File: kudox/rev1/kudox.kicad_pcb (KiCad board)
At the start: 2 copper layers, 143.6 x 129.5 mm, 81 parts, among them K0 KEYSW, K1 KEYSW, K10 KEYSW, K11 KEYSW, K12 KEYSW, K13 KEYSW, K14 KEYSW, K15 KEYSW, K16 KEYSW, K2 KEYSW, K20 KEYSW, K21 KEYSW, K22 KEYSW, K23 KEYSW, K24 KEYSW, K25 KEYSW, K3 KEYSW, K30 KEYSW, K31 KEYSW, K32 KEYSW, K33 KEYSW, K34 KEYSW, K35 KEYSW, K4 KEYSW, K40 KEYSW, K41 KEYSW, K42 KEYSW, K43 KEYSW, K44 KEYSW, K45 KEYSW, K46 KEYSW, K5 KEYSW, U1 ProMicro

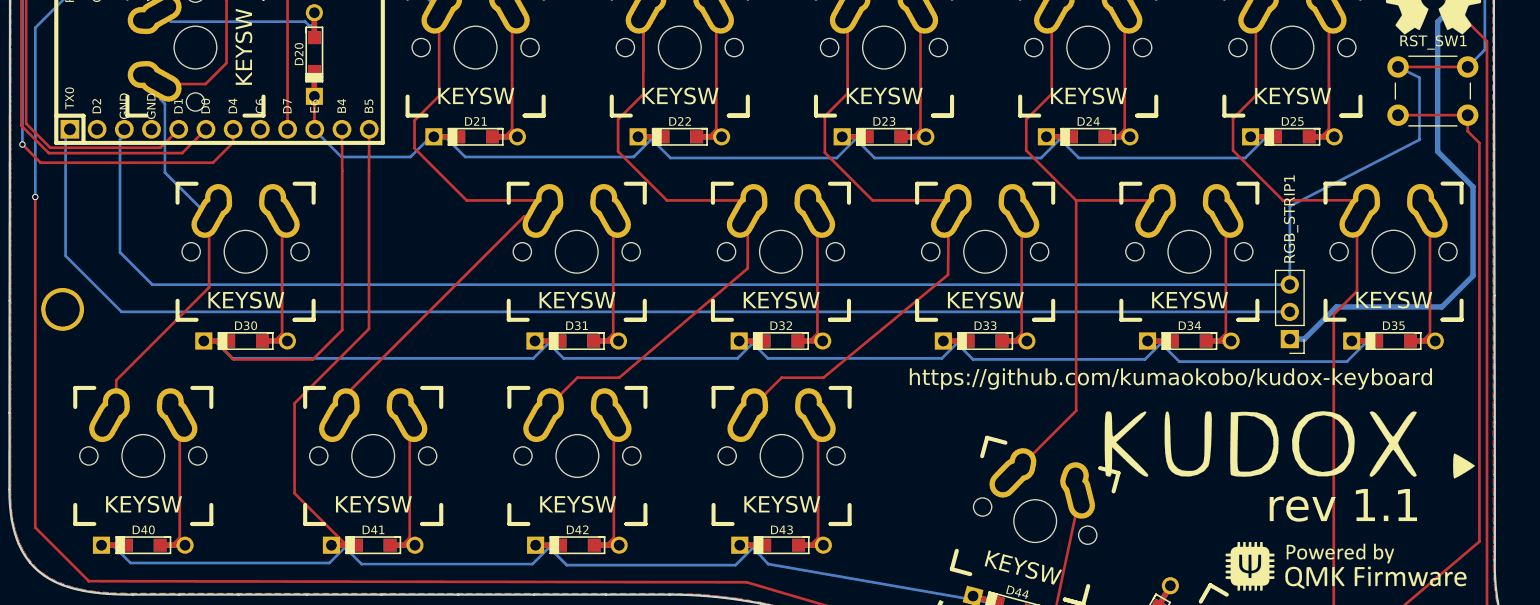
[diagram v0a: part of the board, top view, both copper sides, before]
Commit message: Modified the position of LED pin header. (#34)
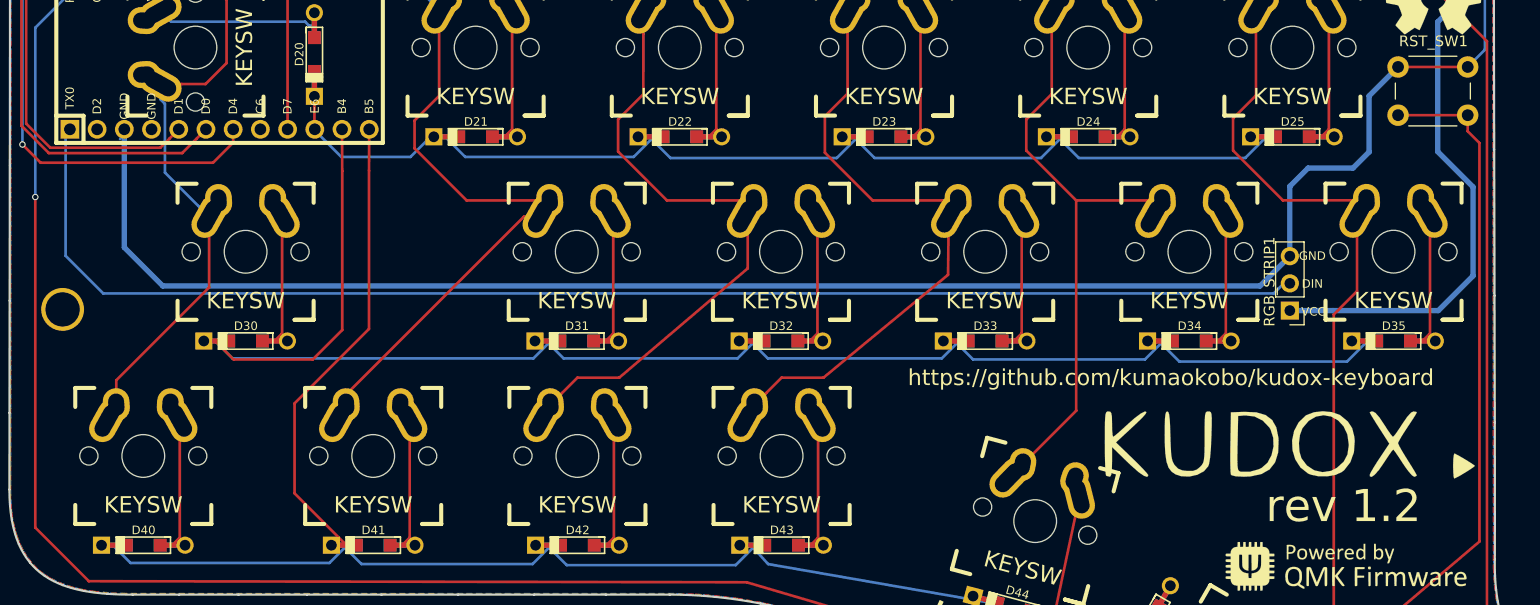
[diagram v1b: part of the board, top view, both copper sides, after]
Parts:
- moved RGB_STRIP1 2.66 mm to (201.3, 123.6)
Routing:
- net GND: track 213.2 -> 210.0 mm
- net VCC: track 262.6 -> 261.5 mm
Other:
- board text added: "rev 1.2"
- board text removed: "rev 1.1"
